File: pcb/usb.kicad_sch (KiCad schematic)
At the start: 8 parts, among them J2 Same Sky UJ20-C-H-G-SMT-P16-TR, U4 USBLC6-2SC6

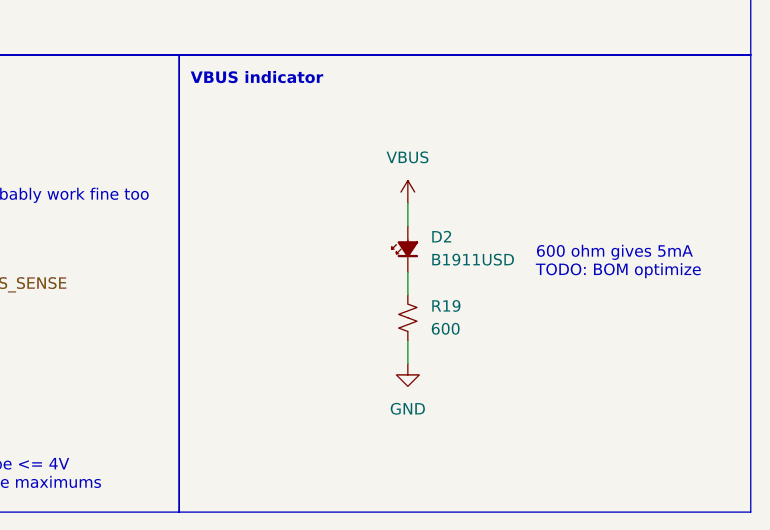
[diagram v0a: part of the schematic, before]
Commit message: Add buck enable switch
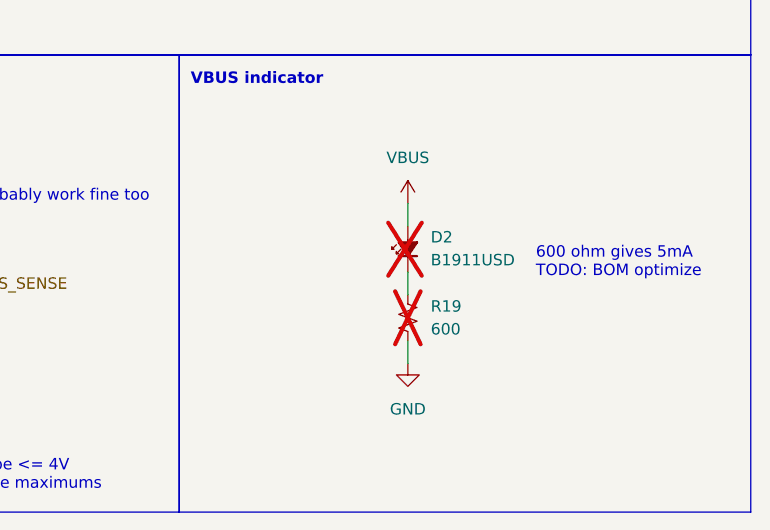
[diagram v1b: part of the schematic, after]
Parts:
- D2, R19: now not fitted
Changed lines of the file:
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@@
 		(dnp no)
 		(fields_autoplaced yes)
-		(property "Reference" "#PWR049"
+		(property "Reference" "#PWR050"
 			(at 25.4 143.51 0)
 			(effects
@@
 			(project ""
 				(path "/1f4fd4ed-9886-4375-a5ac-dc32d5760936/ca842921-3489-4085-9fee-8380a44600c3"
-					(reference "#PWR049")
+					(reference "#PWR050")
 					(unit 1)
 				)
@@
 		(on_board yes)
 		(dnp no)
-		(property "Reference" "#PWR051"
+		(property "Reference" "#PWR052"
 			(at 69.85 87.63 0)
 			(effects
@@
 			(project "airbrake_mod"
 				(path "/1f4fd4ed-9886-4375-a5ac-dc32d5760936/ca842921-3489-4085-9fee-8380a44600c3"
-					(reference "#PWR051")
+					(reference "#PWR052")
 					(unit 1)
 				)
@@
 		(exclude_from_sim no)
 		(in_bom yes)
-		(on_board yes)
-		(dnp no)
+		(on_board no)
+		(dnp yes)
 		(fields_autoplaced yes)
 		(property "Reference" "R19"
@@
 		(dnp no)
 		(fields_autoplaced yes)
-		(property "Reference" "#PWR055"
+		(property "Reference" "#PWR056"
 			(at 88.9 142.24 0)
 			(effects
@@
 			(project "airbrake_mod"
 				(path "/1f4fd4ed-9886-4375-a5ac-dc32d5760936/ca842921-3489-4085-9fee-8380a44600c3"
-					(reference "#PWR055")
+					(reference "#PWR056")
 					(unit 1)
 				)
@@
 		(exclude_from_sim no)
 		(in_bom yes)
-		(on_board yes)
-		(dnp no)
+		(on_board no)
+		(dnp yes)
 		(fields_autoplaced yes)
 		(property "Reference" "D2"
@@
 		(dnp no)
 		(fields_autoplaced yes)
-		(property "Reference" "#PWR048"
+		(property "Reference" "#PWR049"
 			(at 25.4 120.65 0)
 			(effects
@@
 			(project "airbrake_mod"
 				(path "/1f4fd4ed-9886-4375-a5ac-dc32d5760936/ca842921-3489-4085-9fee-8380a44600c3"
-					(reference "#PWR048")
+					(reference "#PWR049")
 					(unit 1)
 				)
@@
 		(dnp no)
 		(fields_autoplaced yes)
-		(property "Reference" "#PWR052"
+		(property "Reference" "#PWR053"
 			(at 88.9 39.37 0)
 			(effects
@@
 			(project "airbrake_mod"
 				(path "/1f4fd4ed-9886-4375-a5ac-dc32d5760936/ca842921-3489-4085-9fee-8380a44600c3"
-					(reference "#PWR052")
+					(reference "#PWR053")
 					(unit 1)
 				)
@@
 		(dnp no)
 		(fields_autoplaced yes)
-		(property "Reference" "#PWR054"
+		(property "Reference" "#PWR055"
 			(at 88.9 121.92 0)
 			(effects
@@
 			(project "airbrake_mod"
 				(path "/1f4fd4ed-9886-4375-a5ac-dc32d5760936/ca842921-3489-4085-9fee-8380a44600c3"
-					(reference "#PWR054")
+					(reference "#PWR055")
 					(unit 1)
 				)
@@
 		(dnp no)
 		(fields_autoplaced yes)
-		(property "Reference" "#PWR053"
+		(property "Reference" "#PWR054"
 			(at 88.9 87.63 0)
 			(effects
@@
 			(project "airbrake_mod"
 				(path "/1f4fd4ed-9886-4375-a5ac-dc32d5760936/ca842921-3489-4085-9fee-8380a44600c3"
-					(reference "#PWR053")
+					(reference "#PWR054")
 					(unit 1)
 				)
@@
 		(dnp no)
 		(fields_autoplaced yes)
-		(property "Reference" "#PWR050"
+		(property "Reference" "#PWR051"
 			(at 35.56 87.63 0)
 			(effects
@@
 			(project "airbrake_mod"
 				(path "/1f4fd4ed-9886-4375-a5ac-dc32d5760936/ca842921-3489-4085-9fee-8380a44600c3"
-					(reference "#PWR050")
-					(unit 1)
-				)
+					(reference "#PWR051")
+					(unit 1)
+				)

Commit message: Add CUR schematic sheet title block
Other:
- company: (none) -> Clarkson University Rocketry Team
- title: (none) -> Air Brakes Module
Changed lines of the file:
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@@
 	(generator_version "9.0")
 	(paper "A4")
+	(title_block
+		(title "Air Brakes Module")
+		(date "2025-11-23")
+		(company "Clarkson University Rocketry Team")
+	)
 	(rectangle
 		(start 12.7 12.7)
